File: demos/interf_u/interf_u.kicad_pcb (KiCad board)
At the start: 2 copper layers, 115.6 x 108.2 mm, 25 parts, among them P1 DB25FEMELLE, U1 74LS245, U2 74LS688, U3 74LS541, U5 628128, U8 EP600, U9 4003APG120, X1 8MHz

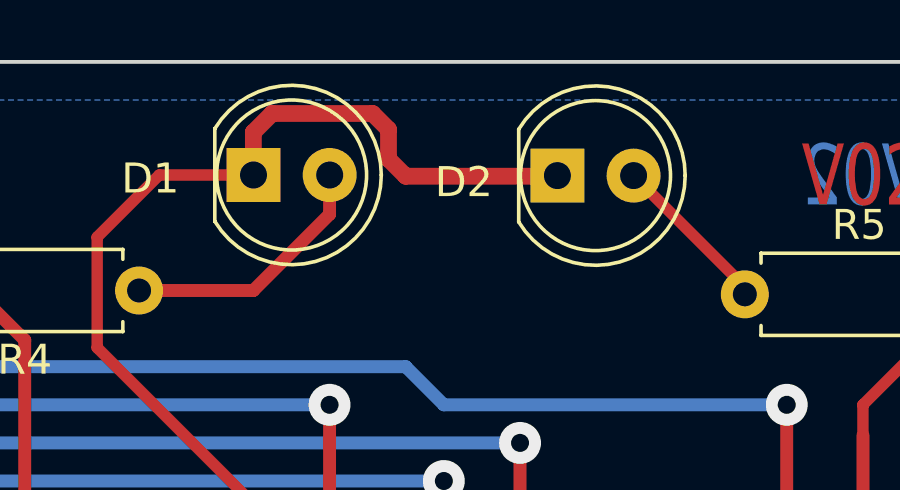
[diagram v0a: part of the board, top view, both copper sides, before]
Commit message: feat: update kicad to 9.0.0+dfsg-1
Signed-off-by: lhdjply <lhdjply@126.com>
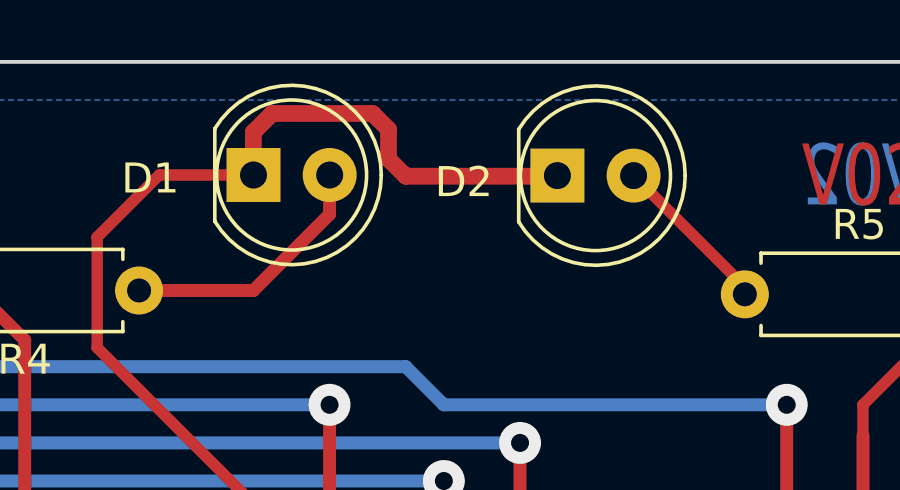
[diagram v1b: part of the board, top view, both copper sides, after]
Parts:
- C1, C4, C5, C6: footprint Capacitor_THT:CP_Axial_L10.0mm_D4.5mm_P15.00mm_Horizontal -> interf_u:CP_Axial_L10.0mm_D4.5mm_P15.00mm_Horizontal
- C2, C3: footprint Capacitor_THT:C_Disc_D3.0mm_W2.0mm_P2.50mm -> interf_u:C_Disc_D3.0mm_W2.0mm_P2.50mm
- D1, D2: footprint LED_THT:LED_D5.0mm -> interf_u:LED_D5.0mm
- JP1: footprint Connector_PinHeader_2.54mm:PinHeader_2x08_P2.54mm_Vertical -> interf_u:PinHeader_2x08_P2.54mm_Vertical
- P1: footprint Connector_Dsub:DSUB-25_Female_Horizontal_P2.77x2.84mm_EdgePinOffset9.90mm_Housed_MountingHolesOffset11.32mm -> interf_u:DSUB-25_Female_Horizontal_P2.77x2.84mm_EdgePinOffset9.90mm_Housed_MountingHolesOffset11.32mm
- R1, R2, R3, R4, R5: footprint Resistor_THT:R_Axial_DIN0207_L6.3mm_D2.5mm_P7.62mm_Horizontal -> interf_u:R_Axial_DIN0207_L6.3mm_D2.5mm_P7.62mm_Horizontal
- RR1: footprint Resistor_THT:R_Array_SIP10 -> interf_u:R_Array_SIP10
- U1, U2, U3: footprint Package_DIP:DIP-20_W7.62mm -> interf_u:DIP-20_W7.62mm
- U5: footprint Package_DIP:DIP-32_W15.24mm -> interf_u:DIP-32_W15.24mm
- U8: footprint Package_DIP:DIP-24_W7.62mm -> interf_u:DIP-24_W7.62mm
- X1: footprint Crystal:Crystal_HC18-U_Horizontal -> interf_u:Crystal_HC18-U_Horizontal
